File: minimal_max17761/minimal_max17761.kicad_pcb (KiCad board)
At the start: 4 copper layers, 31.2 x 12.7 mm, 24 parts, among them J1 FW-02-03-G-D-085-155, J2 FW-02-03-G-D-085-155, U1 MAX17761ATC+

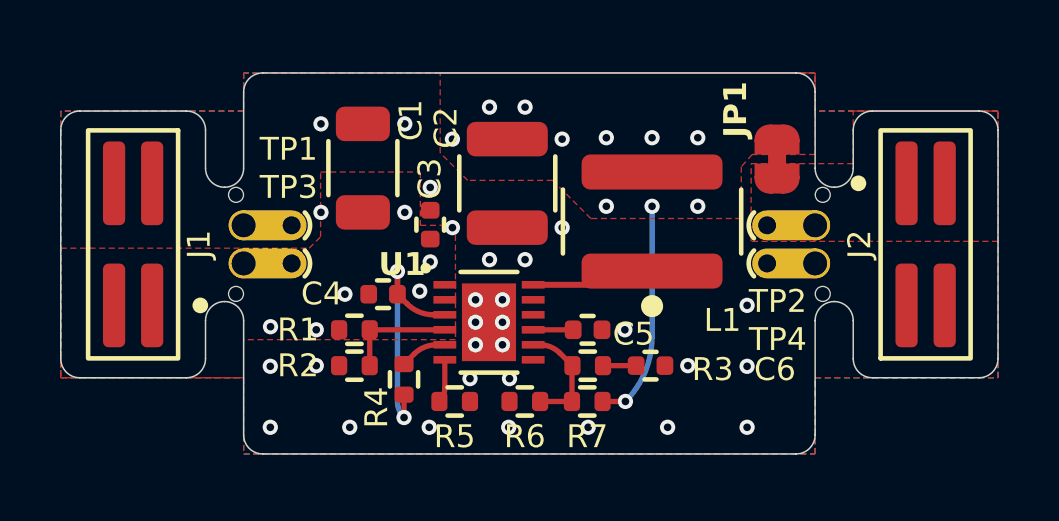
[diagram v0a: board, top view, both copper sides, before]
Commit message: Add new assets and update step file reference for minimal_max17761
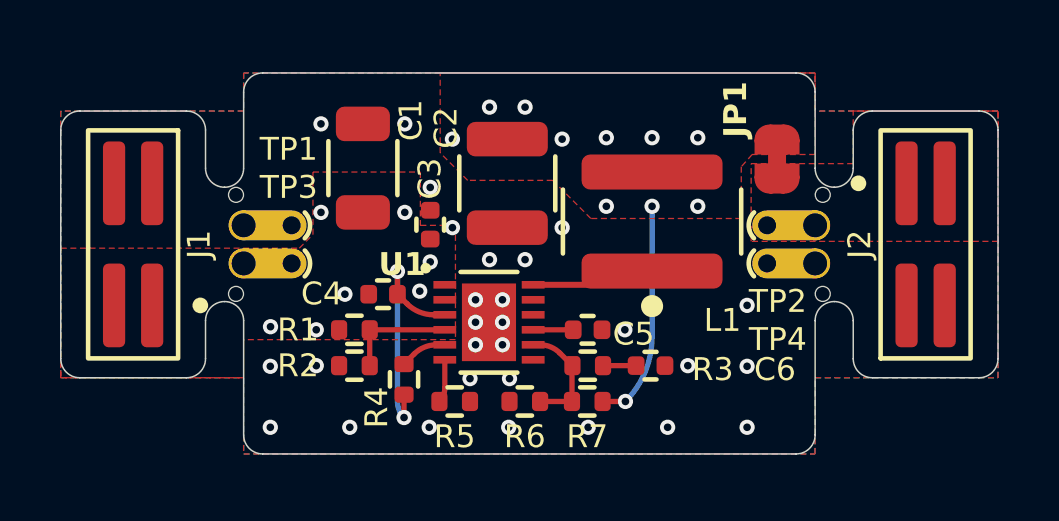
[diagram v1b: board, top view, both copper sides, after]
